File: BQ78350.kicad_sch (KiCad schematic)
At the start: 37 parts, among them J2 Conn_01x04, J3 LED, Q15 BSS84, Q16 2N7002, Q17 2N7002, U2 BQ78350DBT

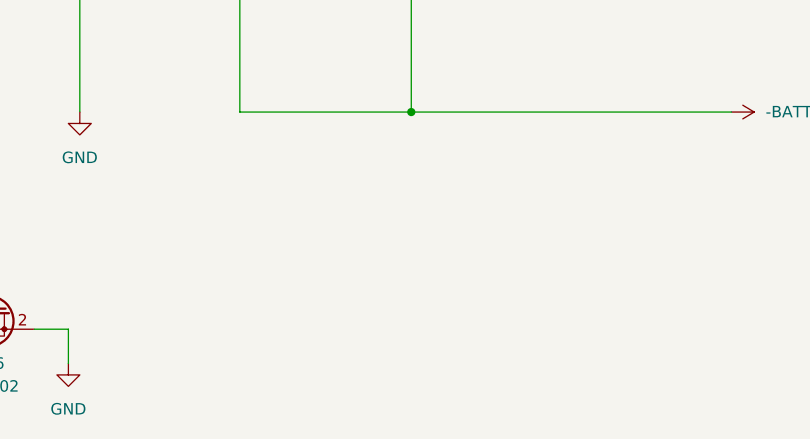
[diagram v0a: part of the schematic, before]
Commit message: Changes Mosfet's package to D2PAK
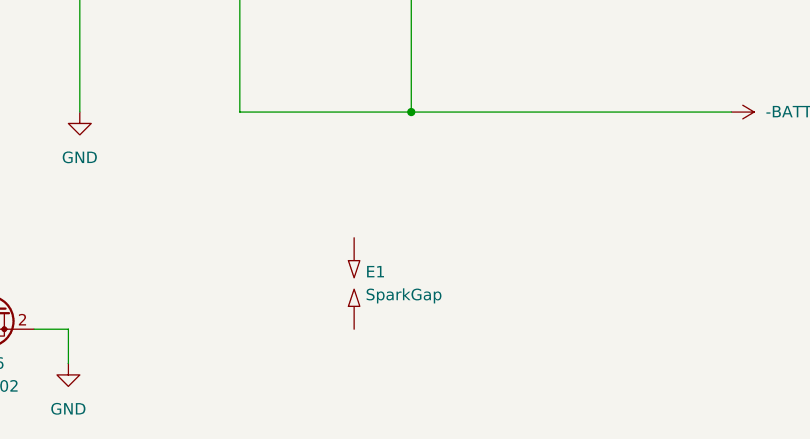
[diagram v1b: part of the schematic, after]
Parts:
- added E1: SparkGap, symbol Device:SparkGap
- C22, C23, C24: footprint (none) -> Capacitor_SMD:C_0603_1608Metric
- D11: footprint (none) -> Diode_SMD:D_PowerDI-123
- J2: footprint (none) -> Connector_JST:JST_XH_B4B-XH-A_1x04_P2.50mm_Vertical
- J3: footprint (none) -> Connector_JST:JST_XH_B6B-XH-A_1x06_P2.50mm_Vertical
- JP1: footprint (none) -> Jumper:SolderJumper-2_P1.3mm_Open_RoundedPad1.0x1.5mm
- NT1, NT2: footprint (none) -> NetTie:NetTie-2_SMD_Pad0.5mm
- R36, R37, R38, R39, R40, R41, R42, R43, R44, R45, R46, R47, R48, R49, R50, R51, R52, R53, R54, R55, R56, R57: footprint (none) -> Resistor_SMD:R_0603_1608Metric
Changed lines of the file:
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@@
 		(shape bidirectional)
 		(at 55.88 86.36 180)
+		(fields_autoplaced yes)
 		(effects
 			(font
@@
 		(shape output)
 		(at 55.88 88.9 180)
+		(fields_autoplaced yes)
 		(effects
 			(font
@@
 		(shape input)
 		(at 55.88 101.6 180)
+		(fields_autoplaced yes)
 		(effects
 			(font
@@
 		(shape output)
 		(at 55.88 96.52 180)
+		(fields_autoplaced yes)
 		(effects
 			(font
@@
 		(shape bidirectional)
 		(at 55.88 91.44 180)
+		(fields_autoplaced yes)
 		(effects
 			(font
@@
 		(shape input)
 		(at 55.88 104.14 180)
+		(fields_autoplaced yes)
 		(effects
 			(font
@@
 			)
 		)
-		(property "Footprint" ""
+		(property "Footprint" "Resistor_SMD:R_0603_1608Metric"
 			(at 66.04 30.48 0)
 			(effects
@@
 			)
 		)
-		(property "Footprint" ""
+		(property "Footprint" "Resistor_SMD:R_0603_1608Metric"
 			(at 148.59 63.5 0)
 			(effects
@@
 			)
 		)
-		(property "Footprint" ""
+		(property "Footprint" "Resistor_SMD:R_0603_1608Metric"
 			(at 153.67 93.98 0)
 			(effects
@@
 			)
 		)
-		(property "Footprint" ""
+		(property "Footprint" "Capacitor_SMD:C_0603_1608Metric"
 			(at 140.97 39.37 0)
 			(effects
@@
 			)
 		)
-		(property "Footprint" ""
+		(property "Footprint" "Resistor_SMD:R_0603_1608Metric"
 			(at 168.91 101.6 0)
 			(effects
@@
 			)
 		)
-		(property "Footprint" ""
+		(property "Footprint" "Resistor_SMD:R_0603_1608Metric"
 			(at 86.36 80.01 0)
 			(effects
@@
 			)
 		)
-		(property "Footprint" ""
+		(property "Footprint" "Resistor_SMD:R_0603_1608Metric"
 			(at 140.97 144.78 0)
 			(effects
@@
 			)
 		)
-		(property "Footprint" ""
+		(property "Footprint" "Resistor_SMD:R_0603_1608Metric"
 			(at 76.2 80.01 0)
 			(effects
@@
 			)
 		)
-		(property "Footprint" ""
+		(property "Footprint" "Resistor_SMD:R_0603_1608Metric"
 			(at 140.97 63.5 0)
 			(effects
@@
 			)
 		)
-		(property "Footprint" ""
+		(property "Footprint" "Resistor_SMD:R_0603_1608Metric"
 			(at 207.01 91.44 0)
 			(effects
@@
 			)
 		)
-		(property "Footprint" ""
+		(property "Footprint" "Connector_JST:JST_XH_B6B-XH-A_1x06_P2.50mm_Vertical"
 			(at 231.14 73.66 0)
 			(effects
@@
 			)
 		)
-		(property "Footprint" ""
+		(property "Footprint" "Resistor_SMD:R_0603_1608Metric"
 			(at 163.83 63.5 0)
 			(effects
@@
 			)
 		)
-		(property "Footprint" ""
+		(property "Footprint" "Resistor_SMD:R_0603_1608Metric"
 			(at 185.42 63.5 0)
 			(effects
@@
 			)
 		)
-		(property "Footprint" ""
+		(property "Footprint" "Resistor_SMD:R_0603_1608Metric"
 			(at 153.67 91.44 0)
 			(effects
@@
 			)
 		)
-		(property "Footprint" ""
+		(property "Footprint" "Resistor_SMD:R_0603_1608Metric"
 			(at 130.81 144.78 0)
 			(effects
@@
 			)
 		)
-		(property "Footprint" ""
+		(property "Footprint" "Resistor_SMD:R_0603_1608Metric"
 			(at 160.02 101.6 0)
 			(effects
@@
 			)
 		)
-		(property "Footprint" ""
+		(property "Footprint" "NetTie:NetTie-2_SMD_Pad0.5mm"
 			(at 102.87 114.3 0)
 			(effects
@@
 			)
 		)
-		(property "Footprint" ""
+		(property "Footprint" "Diode_SMD:D_PowerDI-123"
 			(at 76.2 31.75 0)
 			(effects
@@
 			)
 		)
-		(property "Footprint" ""
+		(property "Footprint" "Resistor_SMD:R_0603_1608Metric"
 			(at 55.88 52.07 0)
 			(effects
@@
 			)
 		)
-		(property "Footprint" ""
+		(property "Footprint" "Resistor_SMD:R_0603_1608Metric"
 			(at 156.21 63.5 0)
 			(effects
@@
 			)
 		)
-		(property "Footprint" ""
+		(property "Footprint" "Resistor_SMD:R_0603_1608Metric"
 			(at 82.55 40.64 0)
 			(effects
@@
 	)
 	(symbol
+		(lib_id "Device:SparkGap")
+		(at 190.5 139.7 90)
+		(unit 1)
+		(exclude_from_sim no)
+		(in_bom yes)
+		(on_board yes)
+		(dnp no)
+		(fields_autoplaced yes)
+		(property "Reference" "E1"
+			(at 191.77 138.4299 90)
+			(effects
+				(font
+					(size 1.27 1.27)
+				)
+				(justify right)
+			)
+		)
+		(property "Value" "SparkGap"
+			(at 191.77 140.9699 90)
+			(effects
+				(font
+					(size 1.27 1.27)
+				)
+				(justify right)
+			)
+		)
+		(property "Footprint" ""
+			(at 192.278 139.7 0)
+			(effects
+				(font
+					(size 1.27 1.27)
+				)
+				(hide yes)
+			)
+		)
+		(property "Datasheet" "~"
+			(at 190.5 139.7 90)
+			(effects
+				(font
+					(size 1.27 1.27)
+				)
+				(hide yes)
+			)
+		)
+		(property "Description" "Spark gap"
+			(at 190.5 139.7 0)
+			(effects
+				(font
+					(size 1.27 1.27)
+				)
+				(hide yes)
+			)
+		)
+		(pin "1"
+		)
+		(pin "2"
+		)
+		(instances
+			(project ""
+				(path "/1b322c88-a1e6-4706-b5ad-2d81e9035abf/f5e36afc-4a94-420d-a8e6-d57c9c557573"
+					(reference "E1")
+					(unit 1)
+				)
+			)
+		)
+	)
+	(symbol
 		(lib_id "Battery_Management:BQ78350DBT")
 		(at 120.65 91.44 0)
@@
 			)
 		)
-		(property "Footprint" ""
+		(property "Footprint" "Resistor_SMD:R_0603_1608Metric"
 			(at 97.79 57.15 0)
 			(effects
@@
 			)
 		)
-		(property "Footprint" ""
+		(property "Footprint" "Capacitor_SMD:C_0603_1608Metric"
 			(at 135.89 110.49 0)
 			(effects
@@
 			)
 		)
-		(property "Footprint" ""
+		(property "Footprint" "Resistor_SMD:R_0603_1608Metric"
 			(at 105.41 62.23 0)
 			(effects
@@
 			)
 		)
-		(property "Footprint" ""
+		(property "Footprint" "Resistor_SMD:R_0603_1608Metric"
 			(at 171.45 63.5 0)
 			(effects
@@
 			)
 		)
-		(property "Footprint" ""
+		(property "Footprint" "Connector_JST:JST_XH_B4B-XH-A_1x04_P2.50mm_Vertical"
 			(at 231.14 91.44 0)
 			(effects
@@
 			)
 		)
-		(property "Footprint" ""
+		(property "Footprint" "Resistor_SMD:R_0603_1608Metric"
 			(at 49.53 73.66 0)
 			(effects
@@
 			)
 		)
-		(property "Footprint" ""
+		(property "Footprint" "Resistor_SMD:R_0603_1608Metric"
 			(at 207.01 93.98 0)
 			(effects
@@
 			)
 		)
-		(property "Footprint" ""
+		(property "Footprint" "Jumper:SolderJumper-2_P1.3mm_Open_RoundedPad1.0x1.5mm"
 			(at 86.36 64.77 0)
 			(effects
@@
 			)
 		)
-		(property "Footprint" ""
+		(property "Footprint" "NetTie:NetTie-2_SMD_Pad0.5mm"
 			(at 102.87 111.76 0)
 			(effects
@@
 			)
 		)
-		(property "Footprint" ""
+		(property "Footprint" "Capacitor_SMD:C_0603_1608Metric"
 			(at 49.53 64.77 0)
 			(effects
